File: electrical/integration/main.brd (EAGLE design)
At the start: 168 x 104 mm, 114 parts

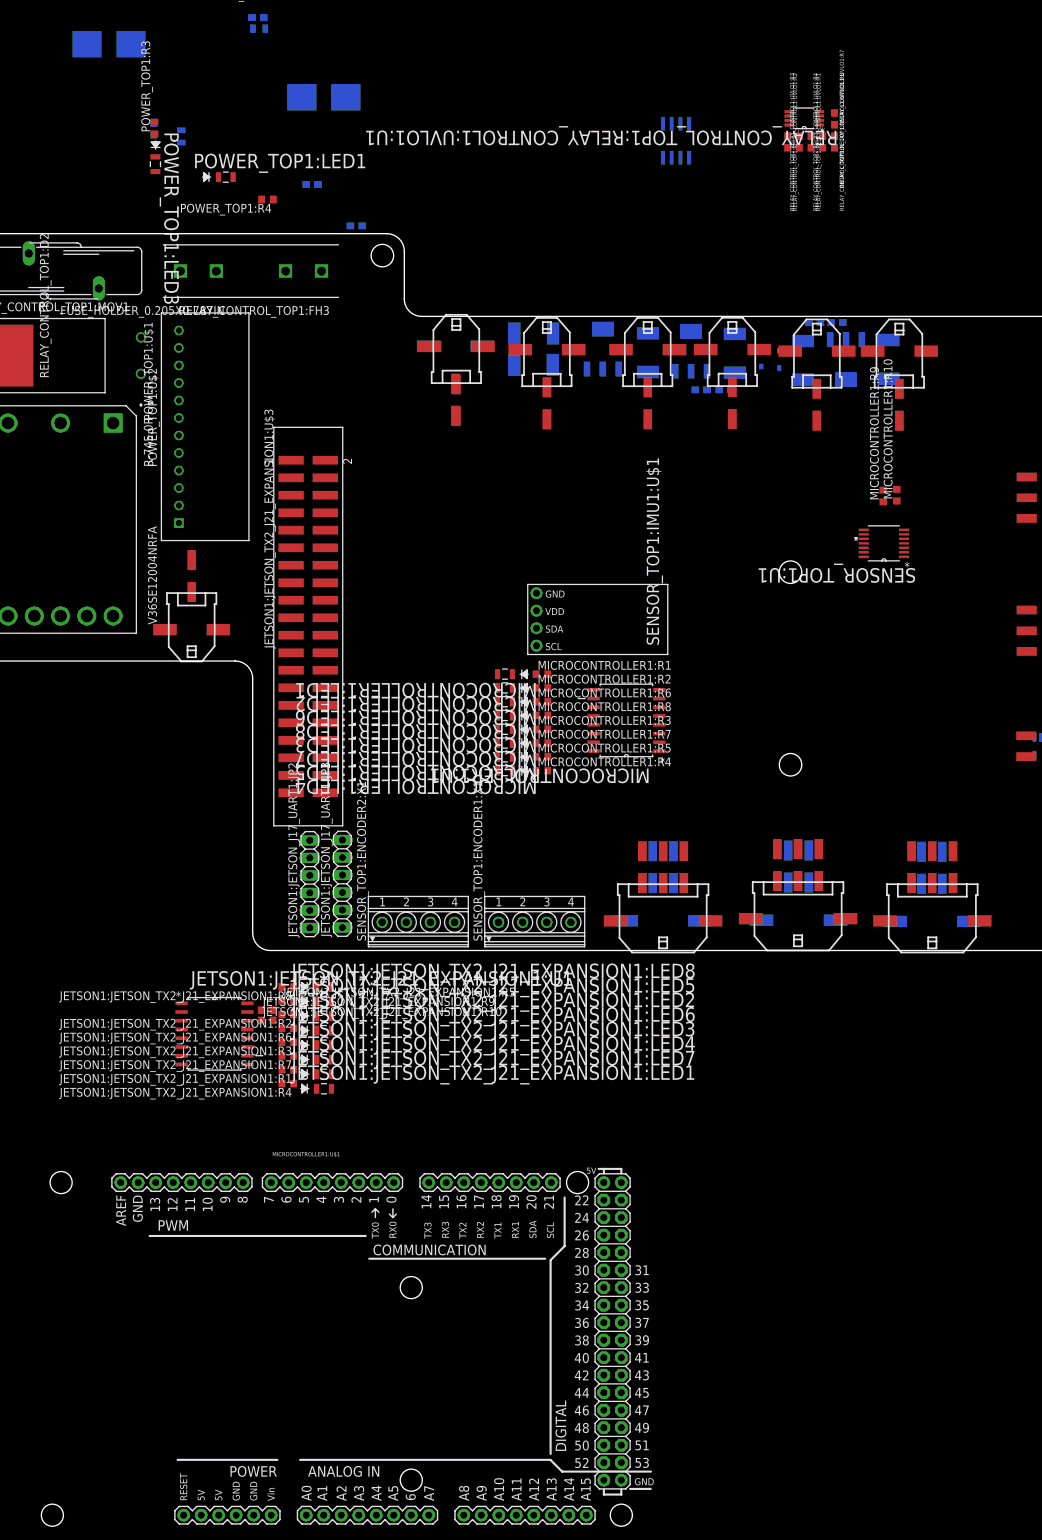
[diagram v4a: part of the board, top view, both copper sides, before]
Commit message: swap coil drive connector polarity for consistency with other connectors
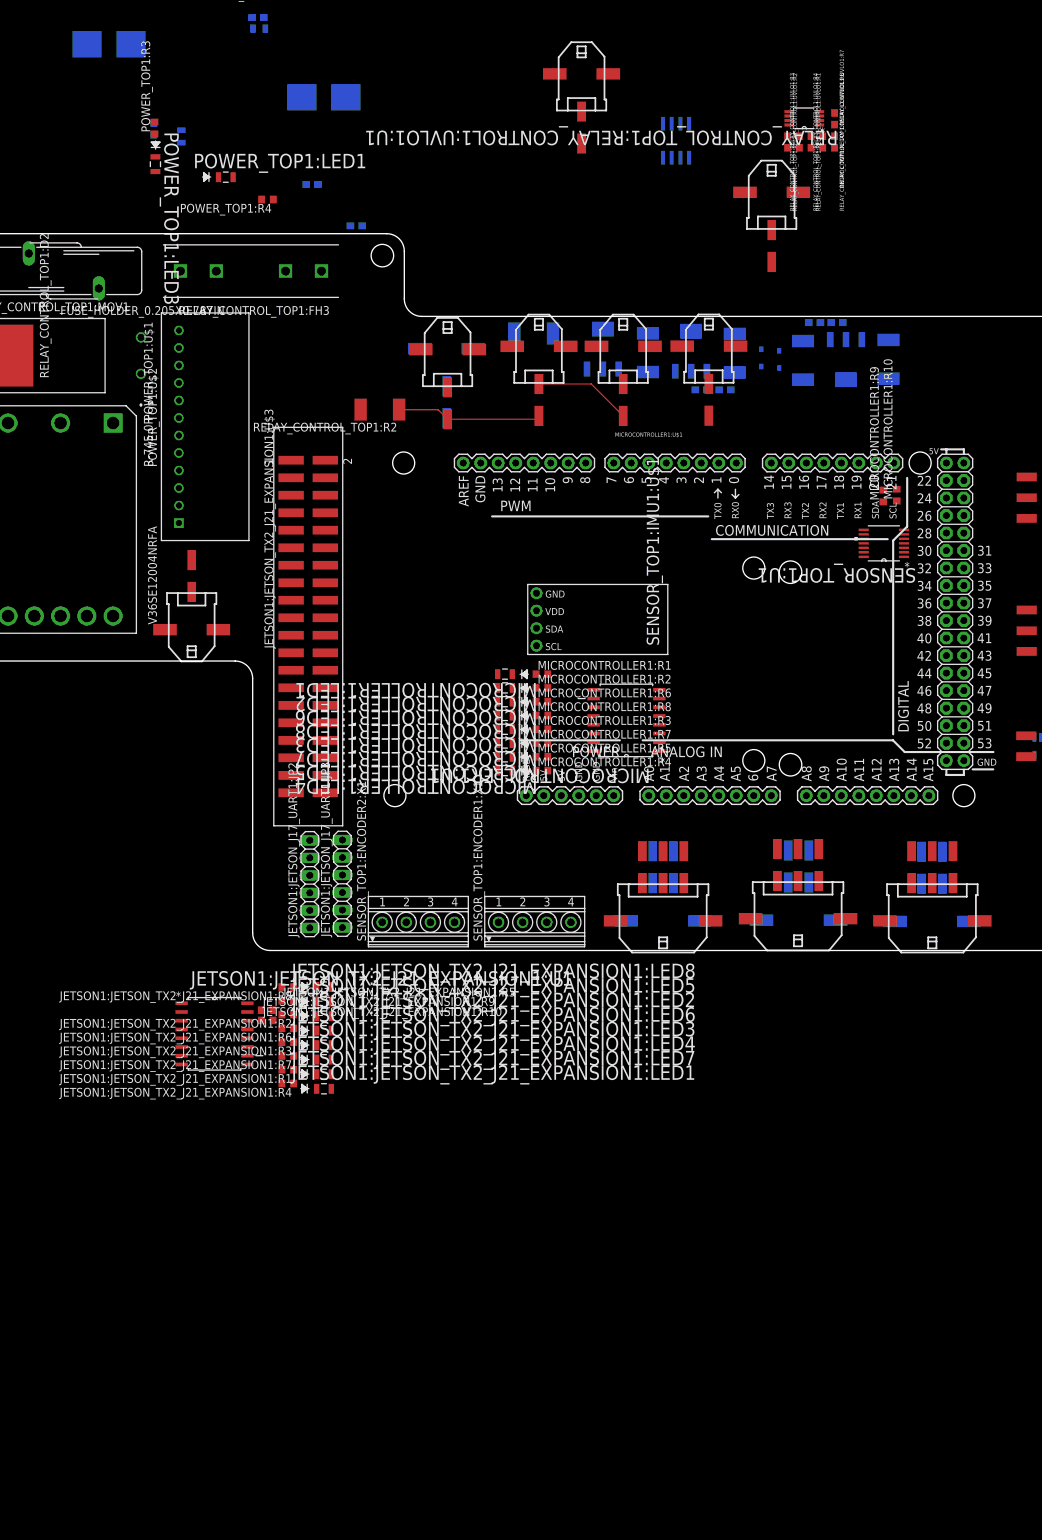
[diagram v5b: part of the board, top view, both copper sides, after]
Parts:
- moved MICROCONTROLLER1:U$1 115.6 mm to (56.2, -45.4)
- moved RELAY_CONTROL_TOP1:RELAY_CONTROL1:JTHR 52.3 mm to (41.5, -4.34)
- moved RELAY_CONTROL_TOP1:JMC 41.1 mm to (47.7, 35.2)
- moved RELAY_CONTROL_TOP1:RELAY_CONTROL1:JESTP 28.1 mm to (53.8, -4.34)
- moved RELAY_CONTROL_TOP1:JDC 23.5 mm to (66.2, -4.32)
- moved RELAY_CONTROL_TOP1:RELAY_CONTROL1:JMOW 23.5 mm to (75.3, 18.0)
- moved RELAY_CONTROL_TOP1:R2 23.2 mm to (18.4, -13.5), flipped to the top
- moved RELAY_CONTROL_TOP1:JBAT 1.43 mm to (28.1, -4.67), flipped to the bottom
- moved RELAY_CONTROL_TOP1:JISO 1.24 mm to (28.3, -4.82), flipped to the top
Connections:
- net RELAY_CONTROL_TOP1:N$2: now also RELAY_CONTROL_TOP1:JMC.P$2; no longer RELAY_CONTROL_TOP1:JMC.P$1
- net RELAY_CONTROL_TOP1:N$3: now also RELAY_CONTROL_TOP1:JDC.P$2; no longer RELAY_CONTROL_TOP1:JDC.P$1
- net RELAY_CONTROL_TOP1:N$4: now also RELAY_CONTROL_TOP1:JMC.P$1; no longer RELAY_CONTROL_TOP1:JMC.P$2
- net RELAY_CONTROL_TOP1:N$6: now also RELAY_CONTROL_TOP1:JDC.P$1; no longer RELAY_CONTROL_TOP1:JDC.P$2
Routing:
- net RELAY_CONTROL_TOP1:36V_RAW: track 0.00 -> 21.1 mm
- net RELAY_CONTROL_TOP1:RELAY_CONTROL1:N$1: track 0.00 -> 14.1 mm

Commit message: move motor encoders to arduino mega interrupts
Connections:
- net MICROCONTROLLER1:10 renamed MICROCONTROLLER1:N$11
- net MICROCONTROLLER1:9 renamed MICROCONTROLLER1:N$10
- net MICROCONTROLLER1:RX0 renamed MICROCONTROLLER1:N$4
- new net MICROCONTROLLER1:23: MICROCONTROLLER1:U$1.23
- new net MICROCONTROLLER1:26: MICROCONTROLLER1:U$1.26
- new net MICROCONTROLLER1:N$5: MICROCONTROLLER1:U$1.4
- new net MICROCONTROLLER1:N$6: MICROCONTROLLER1:U$1.5
- new net MICROCONTROLLER1:N$7: MICROCONTROLLER1:U$1.6
- new net MICROCONTROLLER1:N$8: MICROCONTROLLER1:U$1.7
- new net MICROCONTROLLER1:N$9: MICROCONTROLLER1:U$1.8
- net N$1: no longer MICROCONTROLLER1:U$1.5
- net N$11: no longer MICROCONTROLLER1:U$1.8
- net N$16: no longer MICROCONTROLLER1:U$1.7
- net N$23: no longer MICROCONTROLLER1:U$1.6
- net N$26: no longer MICROCONTROLLER1:U$1.3
- net N$27: no longer MICROCONTROLLER1:U$1.2
- net N$31: now also MICROCONTROLLER1:U$1.2; no longer MICROCONTROLLER1:U$1.23
- net N$33: now also MICROCONTROLLER1:U$1.3; no longer MICROCONTROLLER1:U$1.26
- net N$5: no longer MICROCONTROLLER1:U$1.4
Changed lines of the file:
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@@
 <signal name="N$27">
 <contactref element="MOTOR_TOP1:JDL" pad="P$2"/>
-<contactref element="MICROCONTROLLER1:U$1" pad="2"/>
-<wire x1="116.93" y1="-45.6" x2="65.09" y2="-21.27" width="0" layer="19" extent="1-1"/>
 </signal>
 <signal name="N$26">
 <contactref element="MOTOR_TOP1:JDL" pad="P$3"/>
-<contactref element="MICROCONTROLLER1:U$1" pad="3"/>
-<wire x1="116.93" y1="-48.6" x2="62.55" y2="-21.27" width="0" layer="19" extent="1-1"/>
 </signal>
 <signal name="N$5">
 <contactref element="MOTOR_TOP1:JDR" pad="P$2"/>
-<contactref element="MICROCONTROLLER1:U$1" pad="4"/>
-<wire x1="116.93" y1="-26.3" x2="60.01" y2="-21.27" width="0" layer="19" extent="1-1"/>
 </signal>
 <signal name="N$1">
 <contactref element="MOTOR_TOP1:JDR" pad="P$3"/>
-<contactref element="MICROCONTROLLER1:U$1" pad="5"/>
-<wire x1="116.93" y1="-29.3" x2="57.47" y2="-21.27" width="0" layer="19" extent="1-1"/>
 </signal>
 <signal name="N$23">
 <contactref element="MOTOR_TOP1:X3" pad="P$4"/>
-<contactref element="MICROCONTROLLER1:U$1" pad="6"/>
-<wire x1="101.61" y1="-77.59" x2="54.93" y2="-21.27" width="0" layer="19" extent="1-1"/>
 </signal>
 <signal name="N$16">
 <contactref element="MOTOR_TOP1:X4" pad="P$4"/>
-<contactref element="MICROCONTROLLER1:U$1" pad="7"/>
-<wire x1="82.13" y1="-77.29" x2="52.39" y2="-21.27" width="0" layer="19" extent="1-1"/>
 </signal>
 <signal name="N$11">
 <contactref element="MOTOR_TOP1:X5" pad="P$4"/>
-<contactref element="MICROCONTROLLER1:U$1" pad="8"/>
-<wire x1="62.55" y1="-77.59" x2="48.326" y2="-21.27" width="0" layer="19" extent="1-1"/>
-</signal>
-<signal name="MICROCONTROLLER1:9">
-<contactref element="MICROCONTROLLER1:U$1" pad="9"/>
-</signal>
-<signal name="MICROCONTROLLER1:10">
-<contactref element="MICROCONTROLLER1:U$1" pad="10"/>
 </signal>
 <signal name="MICROCONTROLLER1:11">
@@
 <signal name="N$31">
 <contactref element="SENSOR_TOP1:U1" pad="4"/>
-<contactref element="MICROCONTROLLER1:U$1" pad="23"/>
-<wire x1="94.501" y1="-32.93" x2="103.19" y2="-23.81" width="0" layer="19" extent="1-1"/>
+<contactref element="MICROCONTROLLER1:U$1" pad="2"/>
+<wire x1="65.09" y1="-21.27" x2="94.501" y2="-32.93" width="0" layer="19" extent="1-1"/>
 </signal>
 <signal name="N$32">
@@
 <signal name="N$33">
 <contactref element="SENSOR_TOP1:U1" pad="2"/>
-<contactref element="MICROCONTROLLER1:U$1" pad="26"/>
-<wire x1="94.501" y1="-34.2254" x2="100.65" y2="-28.89" width="0" layer="19" extent="1-1"/>
+<contactref element="MICROCONTROLLER1:U$1" pad="3"/>
+<wire x1="62.55" y1="-21.27" x2="94.501" y2="-34.2254" width="0" layer="19" extent="1-1"/>
 </signal>
 <signal name="N$34">
@@
 <contactref element="MICROCONTROLLER1:R2" pad="2"/>
 <wire x1="42.815" y1="-53.9" x2="59.0052" y2="-57.985" width="0" layer="19" extent="1-1"/>
-</signal>
-<signal name="MICROCONTROLLER1:RX0">
-<contactref element="MICROCONTROLLER1:U$1" pad="1"/>
 </signal>
 <signal name="N$6">
@@
 <wire x1="59.0052" y1="-59.255" x2="42.815" y2="-51.9" width="0" layer="19" extent="1-1"/>
 </signal>
+<signal name="MICROCONTROLLER1:N$4">
+<contactref element="MICROCONTROLLER1:U$1" pad="1"/>
+</signal>
+<signal name="MICROCONTROLLER1:N$5">
+<contactref element="MICROCONTROLLER1:U$1" pad="4"/>
+</signal>
+<signal name="MICROCONTROLLER1:N$6">
+<contactref element="MICROCONTROLLER1:U$1" pad="5"/>
+</signal>
+<signal name="MICROCONTROLLER1:N$7">
+<contactref element="MICROCONTROLLER1:U$1" pad="6"/>
+</signal>
+<signal name="MICROCONTROLLER1:N$8">
+<contactref element="MICROCONTROLLER1:U$1" pad="7"/>
+</signal>
+<signal name="MICROCONTROLLER1:N$9">
+<contactref element="MICROCONTROLLER1:U$1" pad="8"/>
+</signal>
+<signal name="MICROCONTROLLER1:N$10">
+<contactref element="MICROCONTROLLER1:U$1" pad="9"/>
+</signal>
+<signal name="MICROCONTROLLER1:N$11">
+<contactref element="MICROCONTROLLER1:U$1" pad="10"/>
+</signal>
+<signal name="MICROCONTROLLER1:23">
+<contactref element="MICROCONTROLLER1:U$1" pad="23"/>
+</signal>
+<signal name="MICROCONTROLLER1:26">
+<contactref element="MICROCONTROLLER1:U$1" pad="26"/>
+</signal>
 </signals>

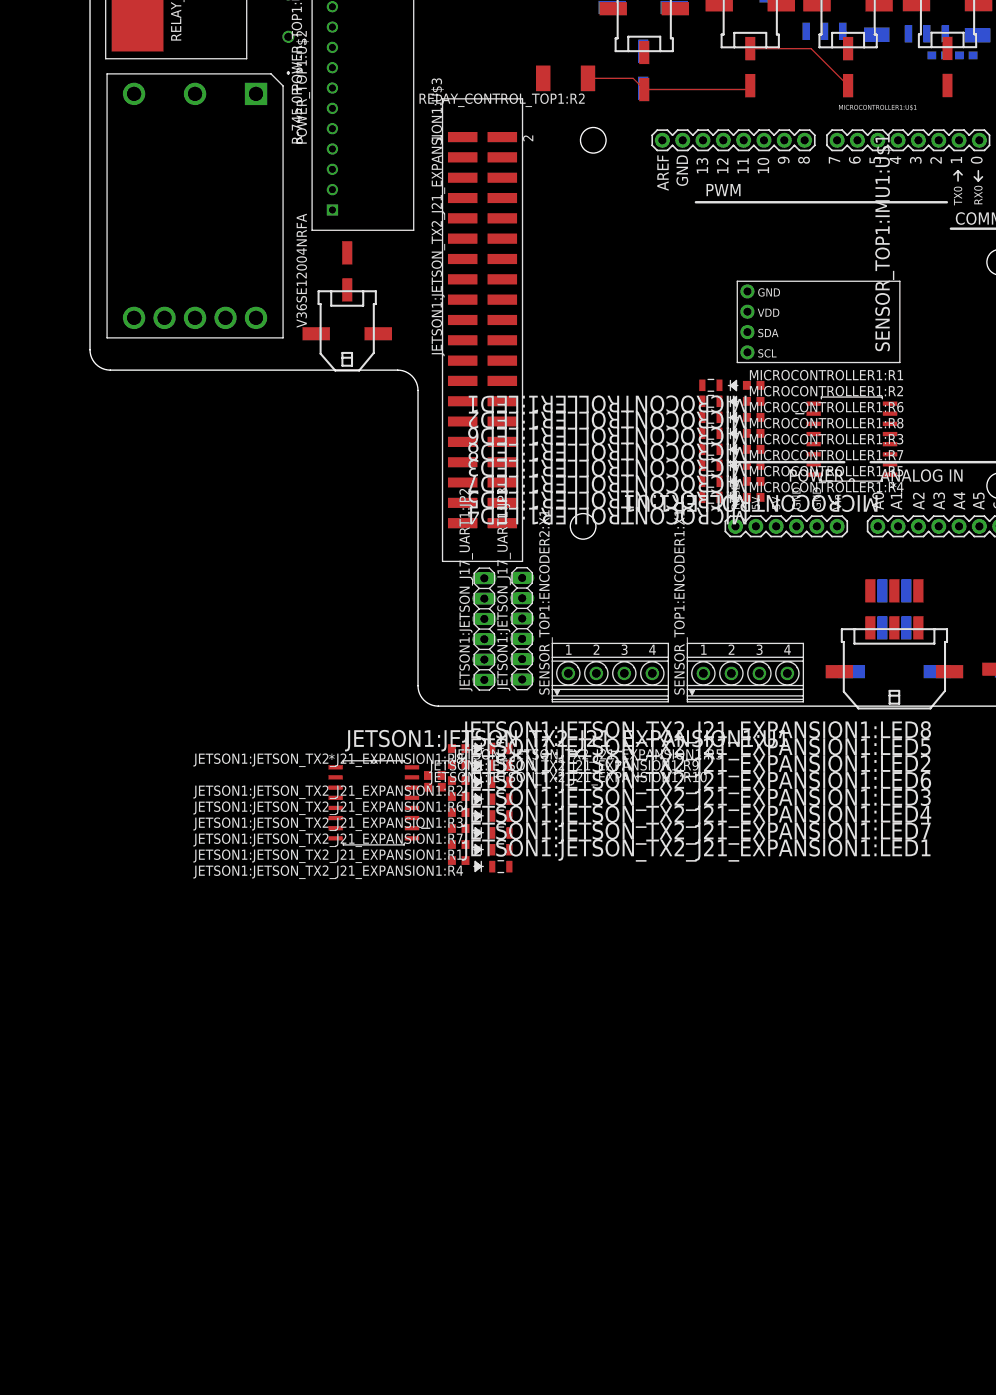
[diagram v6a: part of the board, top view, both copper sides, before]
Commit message: add missing npn base resistor mow en
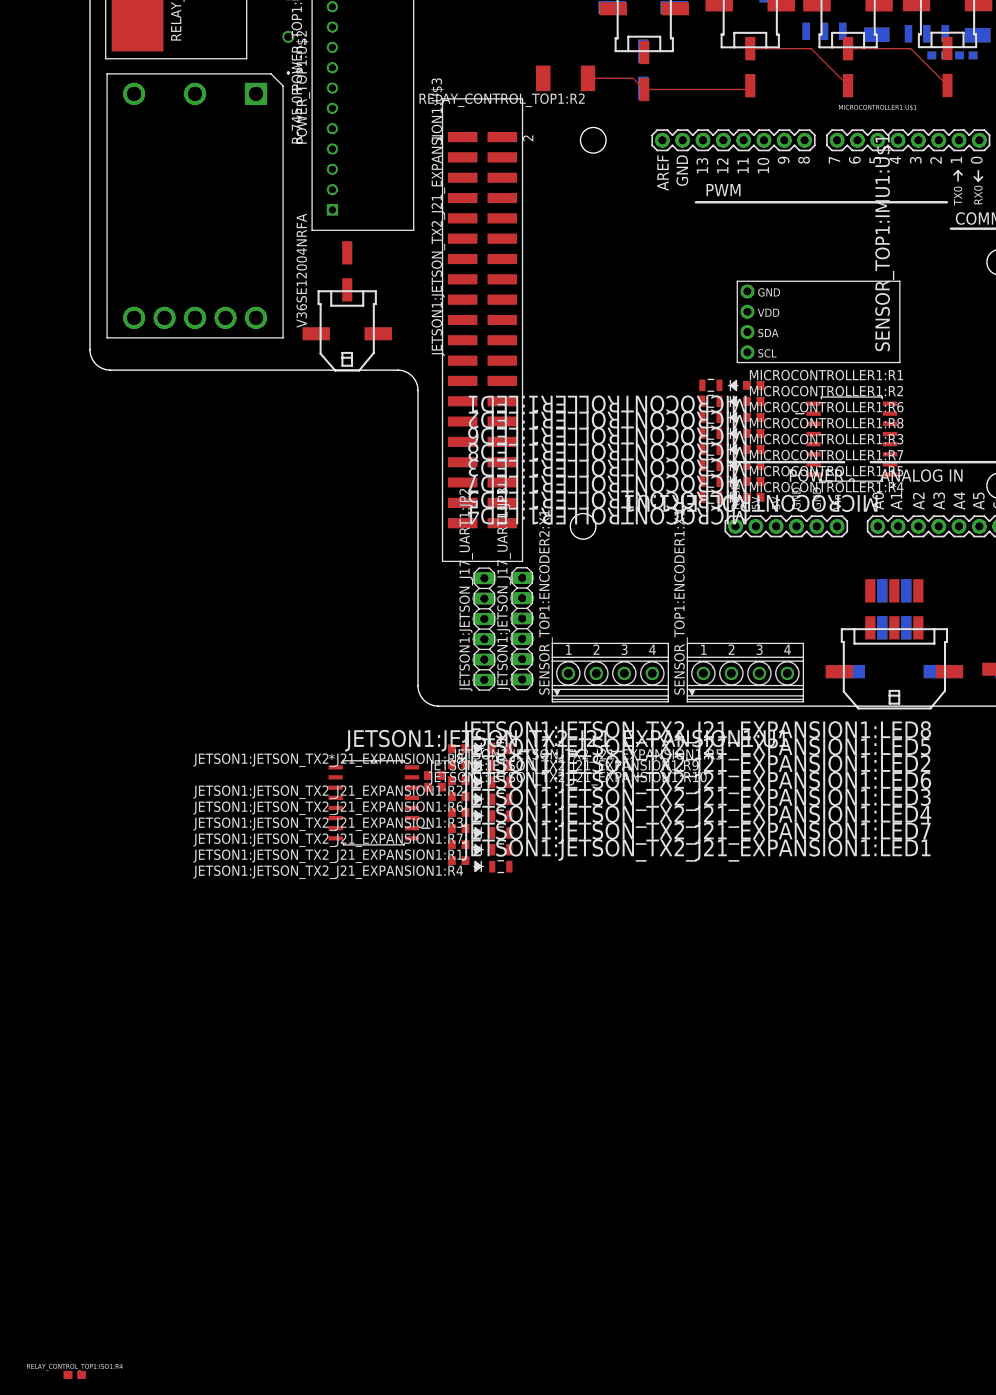
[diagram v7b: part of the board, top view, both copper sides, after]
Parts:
- added RELAY_CONTROL_TOP1:ISO1:R4: 1.20k, SparkFun-Resistors:0603
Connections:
- new net RELAY_CONTROL_TOP1:ISO1:N$3: RELAY_CONTROL_TOP1:ISO1:R1.2, RELAY_CONTROL_TOP1:ISO1:R4.2, RELAY_CONTROL_TOP1:ISO1:U2.3
- net RELAY_CONTROL_TOP1:N$5: now also RELAY_CONTROL_TOP1:ISO1:R4.1; no longer RELAY_CONTROL_TOP1:ISO1:R1.2, RELAY_CONTROL_TOP1:ISO1:U2.3
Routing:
- net RELAY_CONTROL_TOP1:N$3: track 0.00 -> 14.3 mm
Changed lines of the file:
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@@
 <element name="RELAY_CONTROL_TOP1:RELAY_CONTROL1:JMOW" library="con-molex-micro-fit-3_0" package="43045-0209" value="43045-0209" x="75.3" y="18" rot="R180"/>
 <element name="MICROCONTROLLER1:U$1" library="SparkFun-Boards" package="ARDUINO_MEGA" value="ARDUINO_MEGA_R3FULL" x="56.2" y="-45.4"/>
+<element name="RELAY_CONTROL_TOP1:ISO1:R4" library="SparkFun-Resistors" package="0603" value="1.20k" x="-42.9" y="-175.6">
+<attribute name="PROD_ID" value="RES-08413" x="-46.8" y="-175.6" size="1.778" layer="27" display="off"/>
+</element>
 </elements>
 <signals>
@@
 </signal>
 <signal name="RELAY_CONTROL_TOP1:N$5">
-<contactref element="RELAY_CONTROL_TOP1:ISO1:U2" pad="3"/>
-<contactref element="RELAY_CONTROL_TOP1:ISO1:R1" pad="2"/>
 <contactref element="RELAY_CONTROL_TOP1:RELAY_CONTROL1:U$2" pad="1"/>
-<wire x1="156.95" y1="-31.46" x2="154.55" y2="-31.88" width="0" layer="19" extent="1-1"/>
-<wire x1="53.11" y1="-7.64" x2="156.95" y2="-31.46" width="0" layer="19" extent="1-1"/>
+<contactref element="RELAY_CONTROL_TOP1:ISO1:R4" pad="1"/>
+<wire x1="53.11" y1="-7.64" x2="-43.75" y2="-175.6" width="0" layer="19" extent="1-16"/>
 </signal>
 <signal name="RELAY_CONTROL_TOP1:36V_RAW">
@@
 <contactref element="RELAY_CONTROL_TOP1:RELAY_CONTROL1:JMOW" pad="P$2"/>
 <contactref element="RELAY_CONTROL_TOP1:JDC" pad="P$2"/>
+<wire x1="53.76" y1="-9.81" x2="61.58" y2="-9.81" width="0.1524" layer="1"/>
+<wire x1="61.58" y1="-9.81" x2="66.19" y2="-14.42" width="0.1524" layer="1"/>
 <wire x1="76.4" y1="-7.49" x2="75.3" y2="7.9" width="0" layer="19" extent="1-16"/>
 <wire x1="66.19" y1="-14.42" x2="76.4" y2="-7.49" width="0" layer="19" extent="1-16"/>
-<wire x1="53.76" y1="-9.81" x2="66.19" y2="-14.42" width="0" layer="19" extent="1-1"/>
 </signal>
 <signal name="RELAY_CONTROL_TOP1:N$6">
@@
 <contactref element="MICROCONTROLLER1:U$1" pad="26"/>
 </signal>
+<signal name="RELAY_CONTROL_TOP1:ISO1:N$3">
+<contactref element="RELAY_CONTROL_TOP1:ISO1:U2" pad="3"/>
+<contactref element="RELAY_CONTROL_TOP1:ISO1:R1" pad="2"/>
+<contactref element="RELAY_CONTROL_TOP1:ISO1:R4" pad="2"/>
+<wire x1="154.55" y1="-31.88" x2="-42.05" y2="-175.6" width="0" layer="19" extent="1-1"/>
+<wire x1="156.95" y1="-31.46" x2="154.55" y2="-31.88" width="0" layer="19" extent="1-1"/>
+</signal>
 </signals>
